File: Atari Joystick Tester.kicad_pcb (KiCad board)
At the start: 2 copper layers, 67.9 x 52.1 mm, 24 parts, among them J1 Atari_Joystick, J2 Paddle A, J3 Paddle B, J4 Barrel_Jack, J5 Mount, J6 Mount, J7 Mount, J8 Mount, SW1 PADDLE A SEL., SW2 PADDLE B SEL.

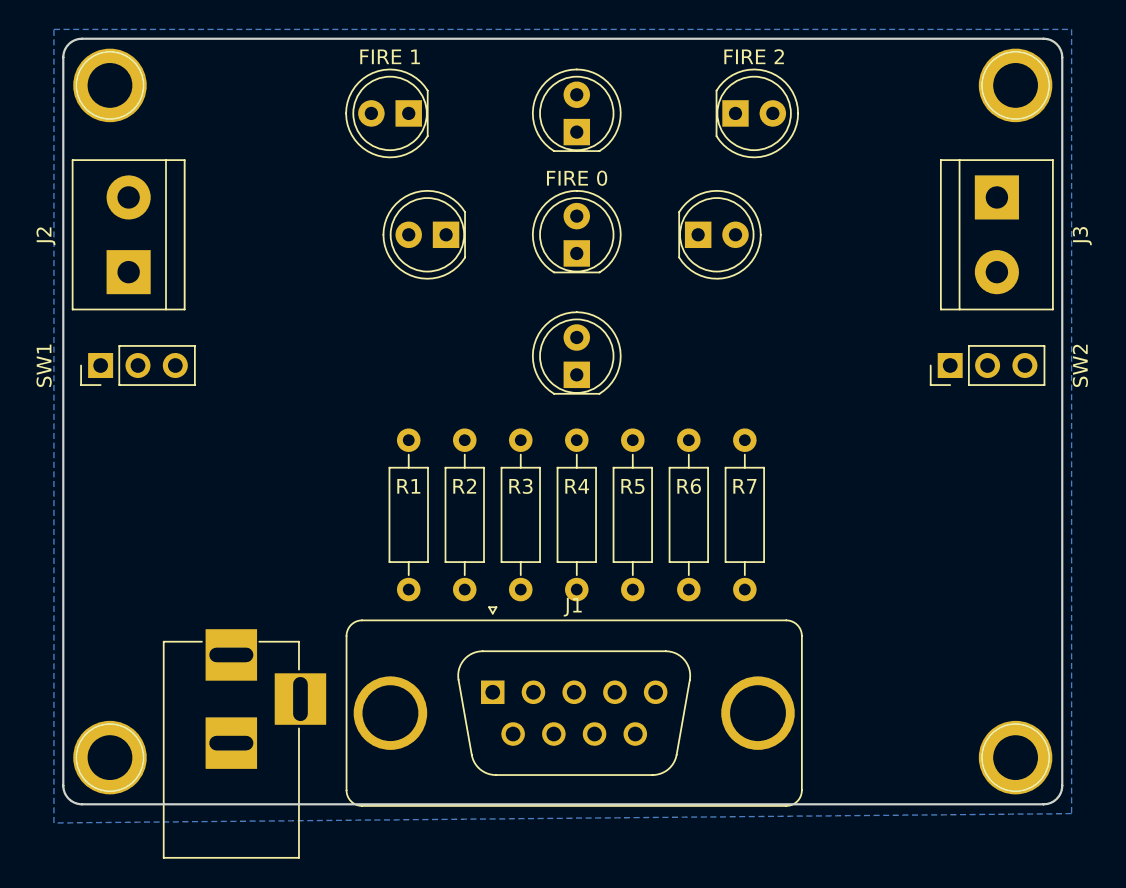
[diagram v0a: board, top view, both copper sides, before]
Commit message: Added wires and exported gerber files.
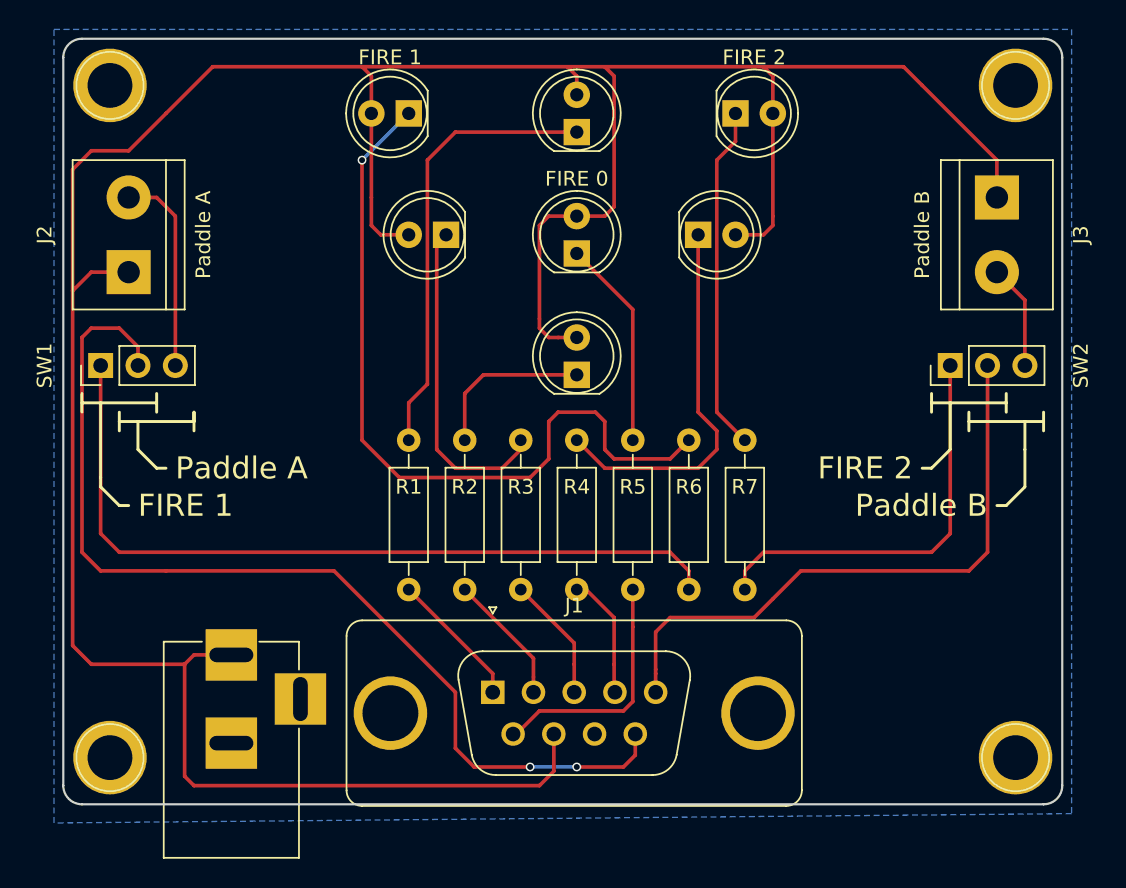
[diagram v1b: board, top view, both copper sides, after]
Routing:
- net VCC: track 0.00 -> 212.1 mm
- net Net-(J1-Pad9): track 0.00 -> 68.2 mm, vias 0 -> 2
- net Net-(R6-Pad2): track 0.00 -> 53.8 mm
- net Net-(D6-Pad1): track 0.00 -> 53.1 mm, vias 0 -> 1
- net Net-(J1-Pad5): track 0.00 -> 41.6 mm
- net Net-(D1-Pad1): track 0.00 -> 30.5 mm
- net Net-(R7-Pad2): track 0.00 -> 27.7 mm
- net Net-(D4-Pad1): track 0.00 -> 26.0 mm
- net Net-(D7-Pad1): track 0.00 -> 23.5 mm
- net Net-(D3-Pad1): track 0.00 -> 22.3 mm
- net Net-(J1-Pad6): track 0.00 -> 16.7 mm
- net Net-(D5-Pad1): track 0.00 -> 14.3 mm
- net Net-(J2-Pad2): track 0.00 -> 13.9 mm
- net Net-(D2-Pad1): track 0.00 -> 11.3 mm
- net Net-(J1-Pad1): track 0.00 -> 9.35 mm
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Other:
- board text added: "Atari Joystick Tester Revision A"
- board text added: "FIRE 1"
- board text added: "FIRE 2"
- board text added: "Paddle A"
- board text added: "Paddle B"
- board text added: "https://hvetebolle.blogspot.com"
